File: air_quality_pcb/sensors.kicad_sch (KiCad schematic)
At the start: 2 parts, among them IC1 SCD41-D-R2, IC2 SGP41-D-R4

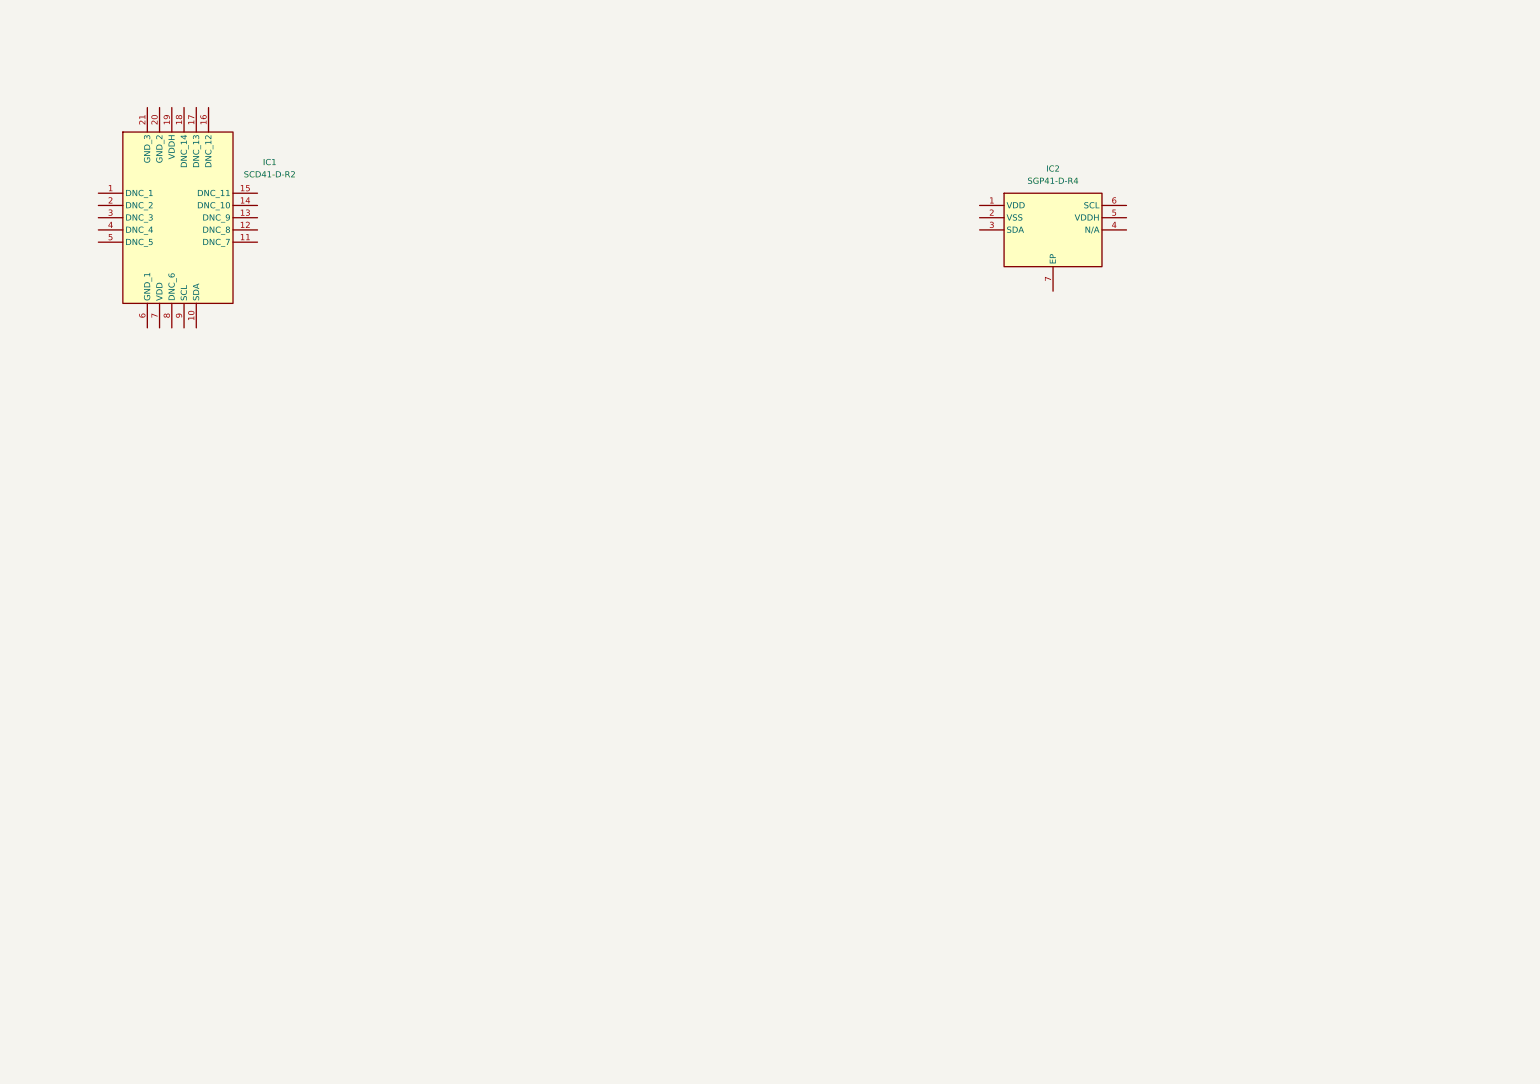
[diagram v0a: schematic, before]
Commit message: added sensors and display example
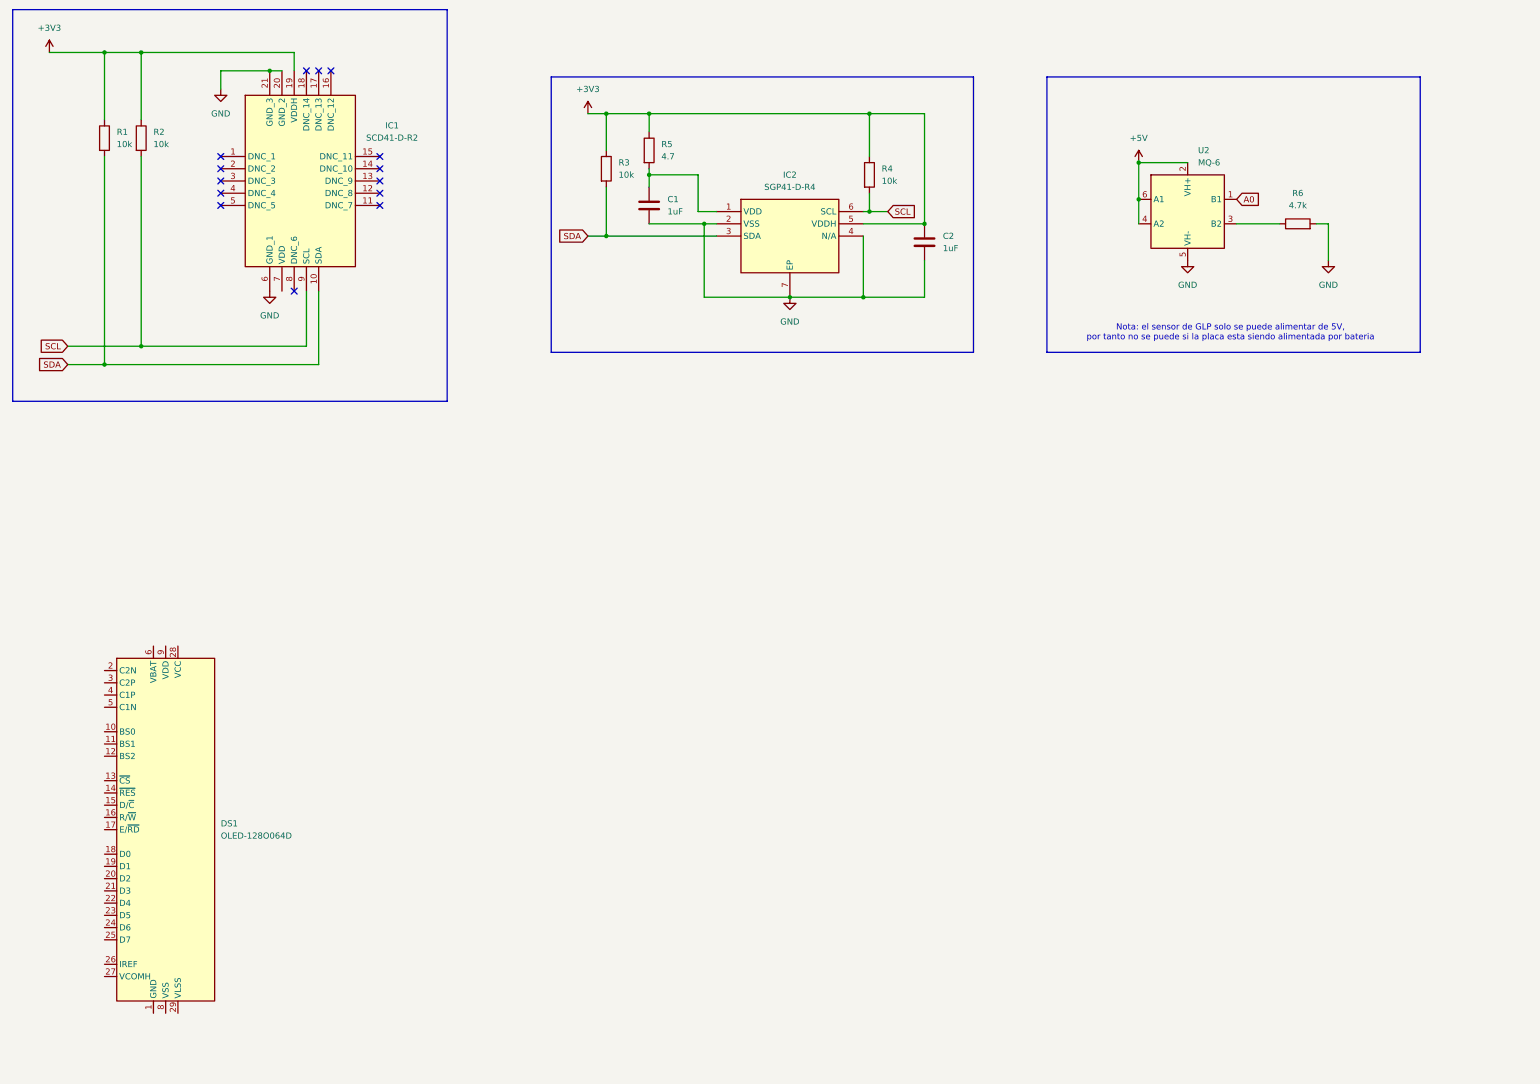
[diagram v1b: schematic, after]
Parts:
- added C1, C2: 1uF, Capacitor_SMD:C_1206_3216Metric, symbol Device:C
- added DS1: OLED-128O064D, Display:OLED-128O064D, symbol Display_Graphic:OLED-128O064D
- added R1, R2, R3, R4: 10k, Resistor_SMD:R_1206_3216Metric, symbol Device:R
- added R5: 4.7, Resistor_SMD:R_1206_3216Metric, symbol Device:R
- added R6: 4.7k, Resistor_SMD:R_1206_3216Metric, symbol Device:R
- added U2: MQ-6, Sensor:MQ-6, symbol Sensor_Gas:MQ-6
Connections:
- net at IC2.1 (VDD): now also C1.1, R5.2
- net GND: now reaches IC2.2 (VSS)
- net GND: now also IC1.20 (GND_2), IC1.21 (GND_3), IC1.6 (GND_1), IC2.4 (N/A), IC2.7 (EP), C1.2, C2.2, R6.2, U2.5 (VH-)
- net SDA: now reaches IC2.3 (SDA)
- net SDA: now also IC1.10 (SDA), R1.2, R3.2
- net +3V3: now reaches IC2.5 (VDDH)
- net +3V3: now also IC1.19 (VDDH), C2.1, R1.1, R2.1, R3.1, R4.1, R5.1
- net SCL: now reaches IC2.6 (SCL)
- net SCL: now also IC1.9 (SCL), R2.2, R4.2
- new net: R6.1, U2.3 (B2)
- new net: DS1.1 (GND), DS1.30 (GND)
- new net +5V: U2.2 (VH+), U2.4 (A2), U2.6 (A1)
- new net A0: U2.1 (B1)
- no-connect marks 0 -> 14
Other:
- note added: "Nota: el sensor de GLP solo se puede alimentar de 5V, por tanto no se puede si la placa esta siendo alimentada por bateria"
- moved on the sheet: IC1, IC2

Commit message: added mq7 sensor and display connector
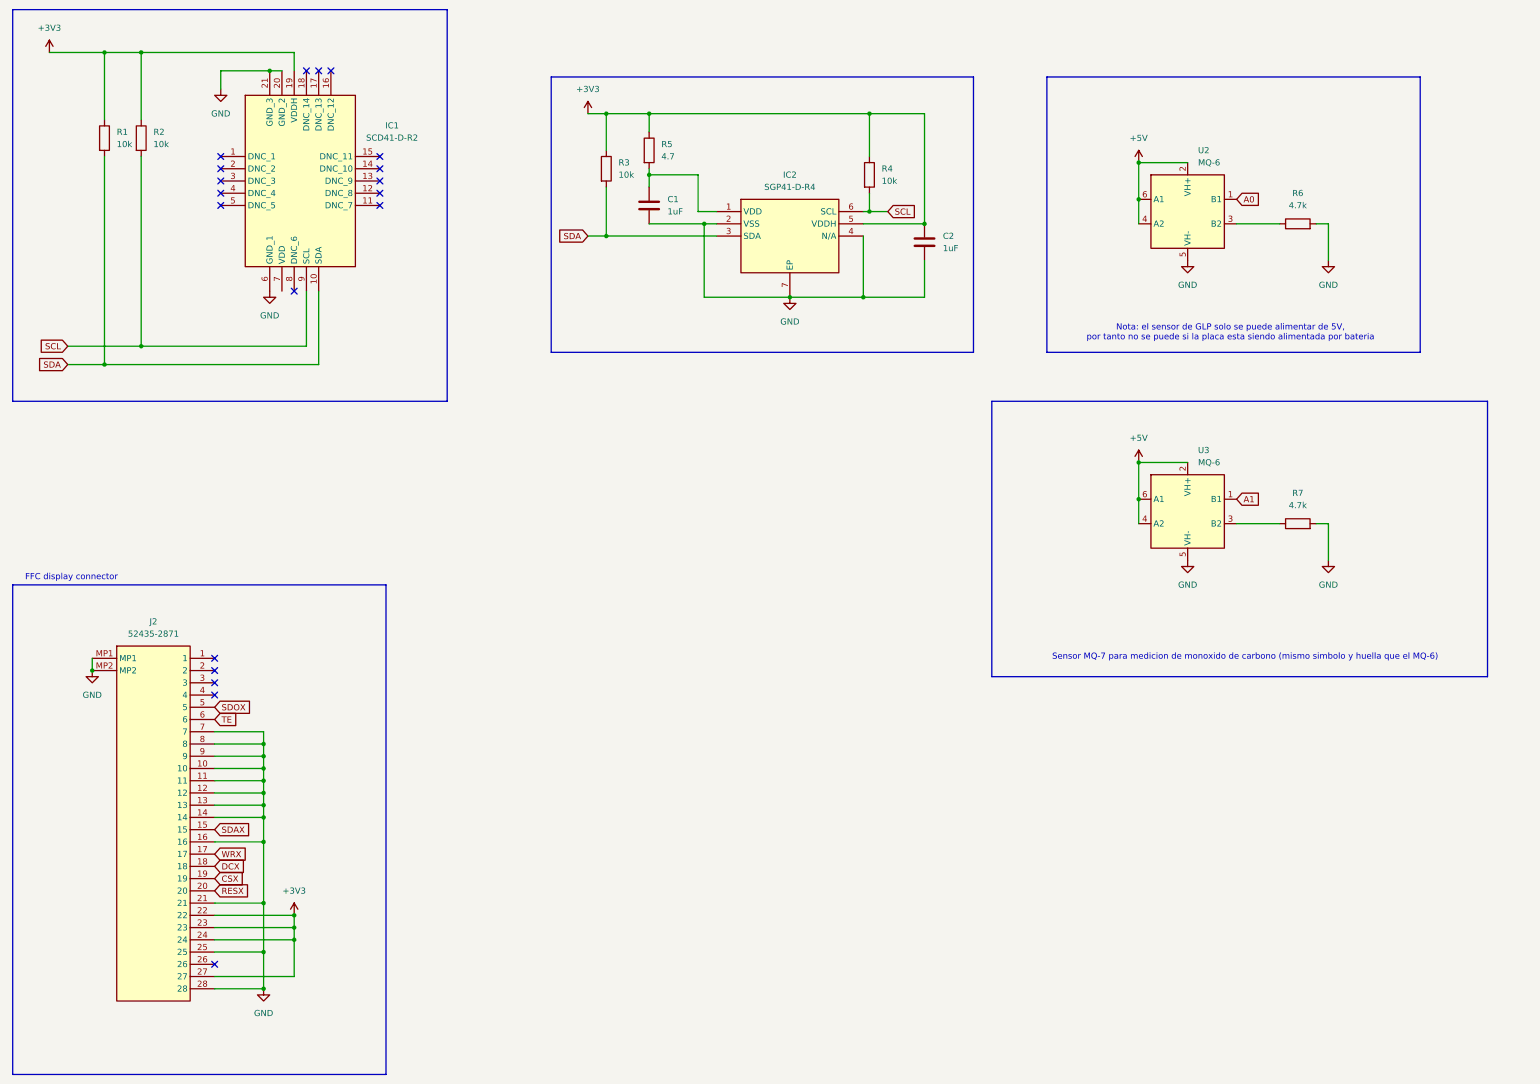
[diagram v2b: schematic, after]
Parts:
- removed DS1: OLED-128O064D, Display:OLED-128O064D, symbol Display_Graphic:OLED-128O064D
- added J2: 52435-2871, project_extras:display_connector, symbol project_extras:52435-2871
- added R7: 4.7k, Resistor_SMD:R_1206_3216Metric, symbol Device:R
- added U3: MQ-6, Sensor:MQ-6, symbol Sensor_Gas:MQ-6
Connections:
- net +3V3: now also J2.22, J2.23, J2.24, J2.27
- net +5V: now also U3.2 (VH+), U3.4 (A2), U3.6 (A1)
- net GND: now also J2.10, J2.11, J2.12, J2.13, J2.14, J2.16, J2.21, J2.25, J2.28, J2.7, J2.8, J2.9, J2.MP1, J2.MP2, R7.2, U3.5 (VH-)
- new net: R7.1, U3.3 (B2)
- new net A1: U3.1 (B1)
- new net CSX: J2.19
- new net DCX: J2.18
- new net RESX: J2.20
- new net SDAX: J2.15
- new net SDOX: J2.5
- new net TE: J2.6
- new net WRX: J2.17
- no-connect marks 14 -> 19
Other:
- note added: "FFC display connector"
- note added: "Sensor MQ-7 para medicion de monoxido de carbono (mismo simbolo y huella que el MQ-6)"

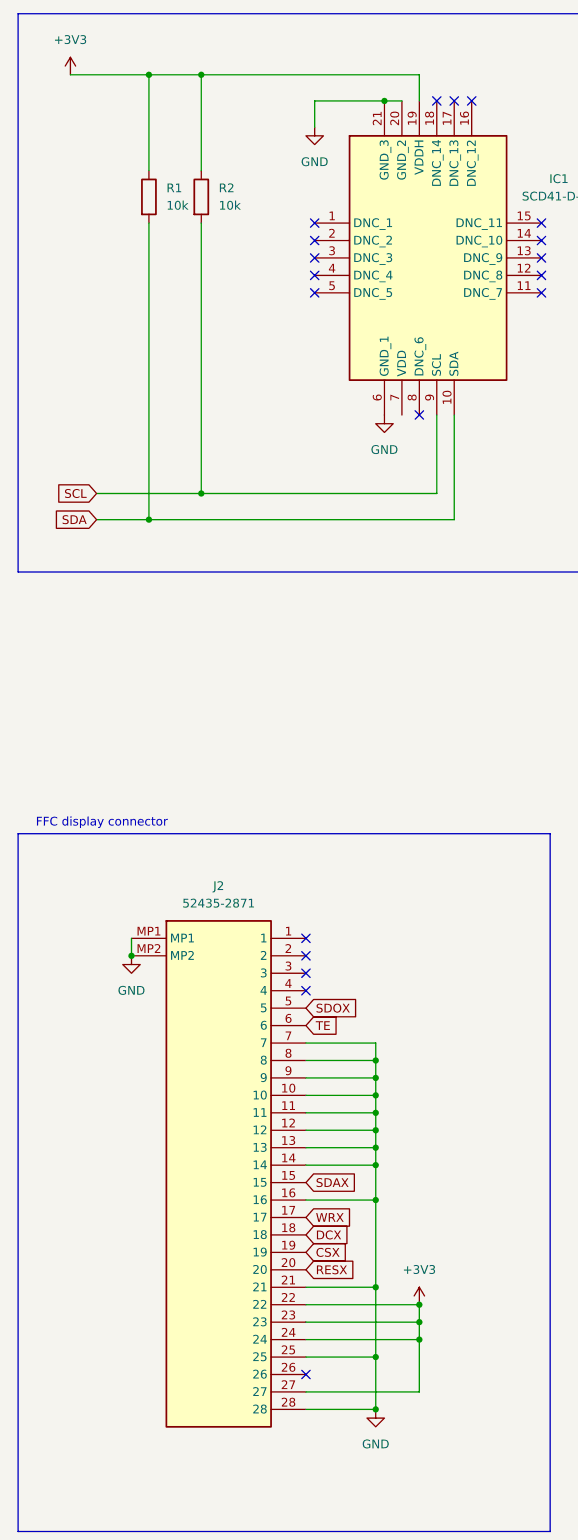
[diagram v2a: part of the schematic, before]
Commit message: finished routing and added more decoupling caps
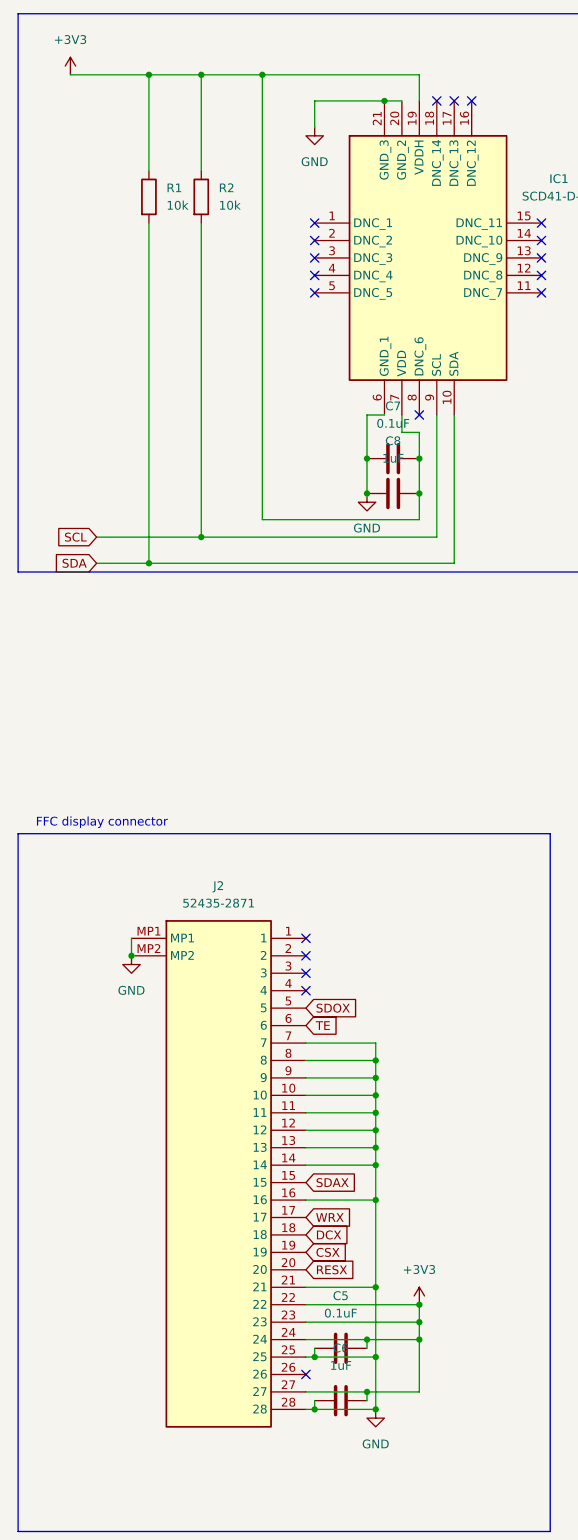
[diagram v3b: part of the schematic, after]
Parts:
- added C5, C7: 0.1uF, Capacitor_SMD:C_1206_3216Metric, symbol Device:C
- added C6, C8: 1uF, Capacitor_SMD:C_1206_3216Metric, symbol Device:C
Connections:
- net +3V3: now also IC1.7 (VDD), C5.1, C6.1, C7.2, C8.2
- net GND: now also C5.2, C6.2, C7.1, C8.1
